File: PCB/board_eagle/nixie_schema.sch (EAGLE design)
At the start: 78 parts, among them IC1 LM2672M, Q1 BC856B, Q2 IRF740S

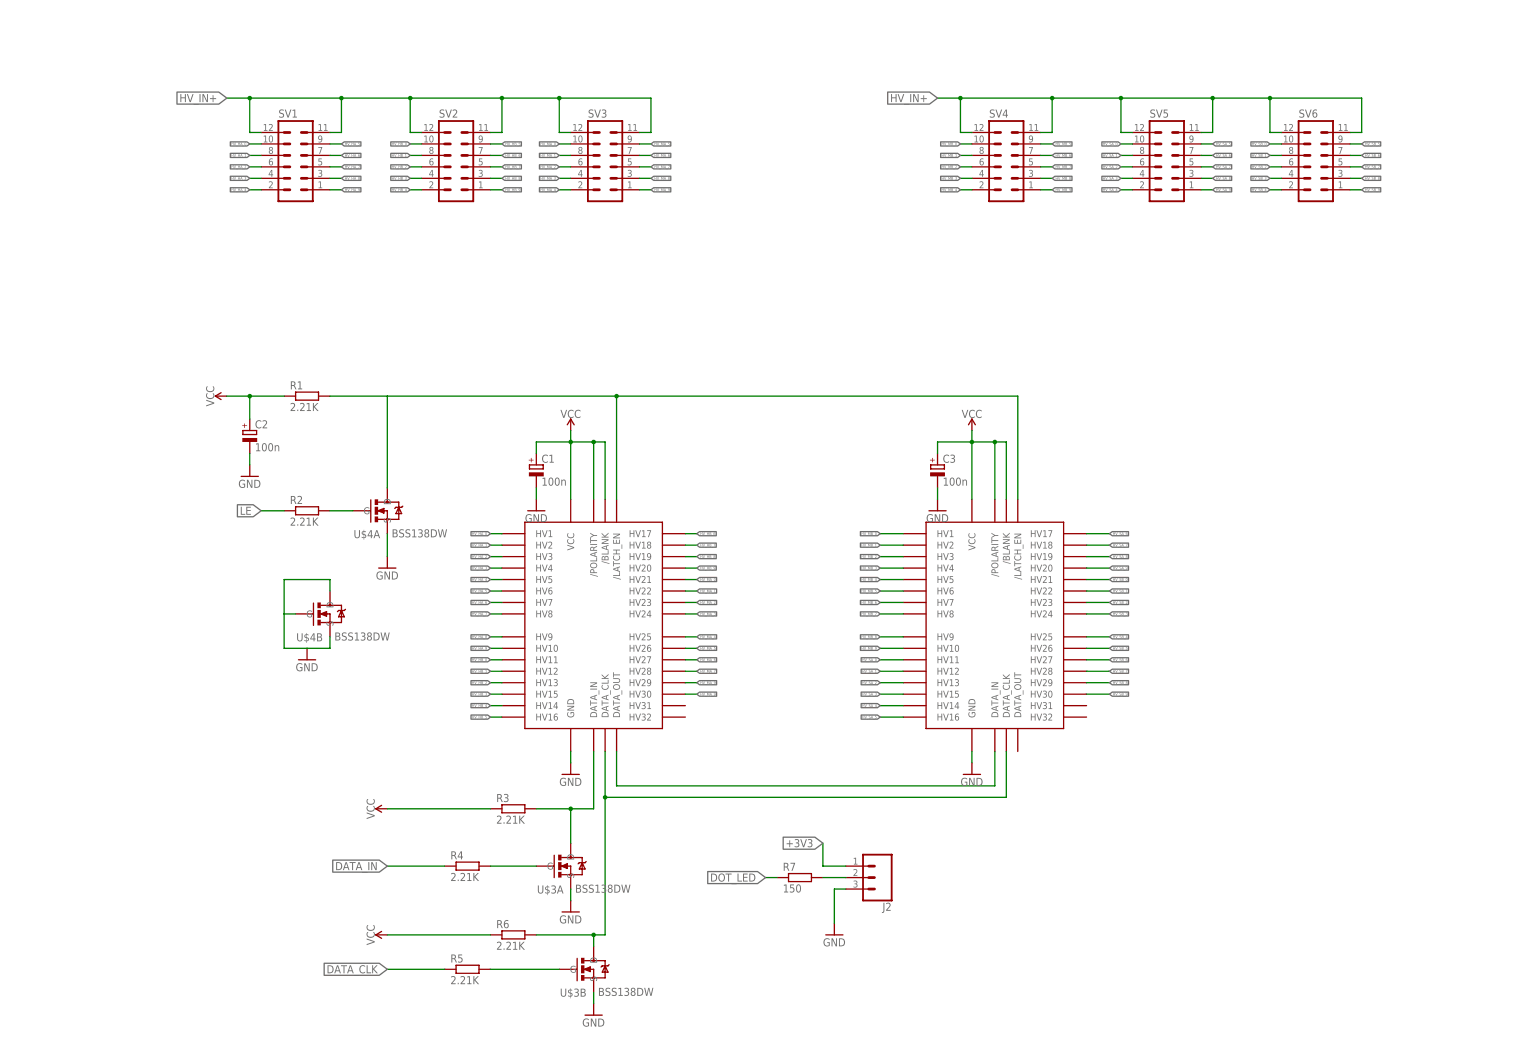
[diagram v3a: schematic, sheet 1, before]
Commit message: Added Buttons
Added 4 buttons and two strip for connectors. buttons are on the last
alb gpios. removed connections for DOT_LED
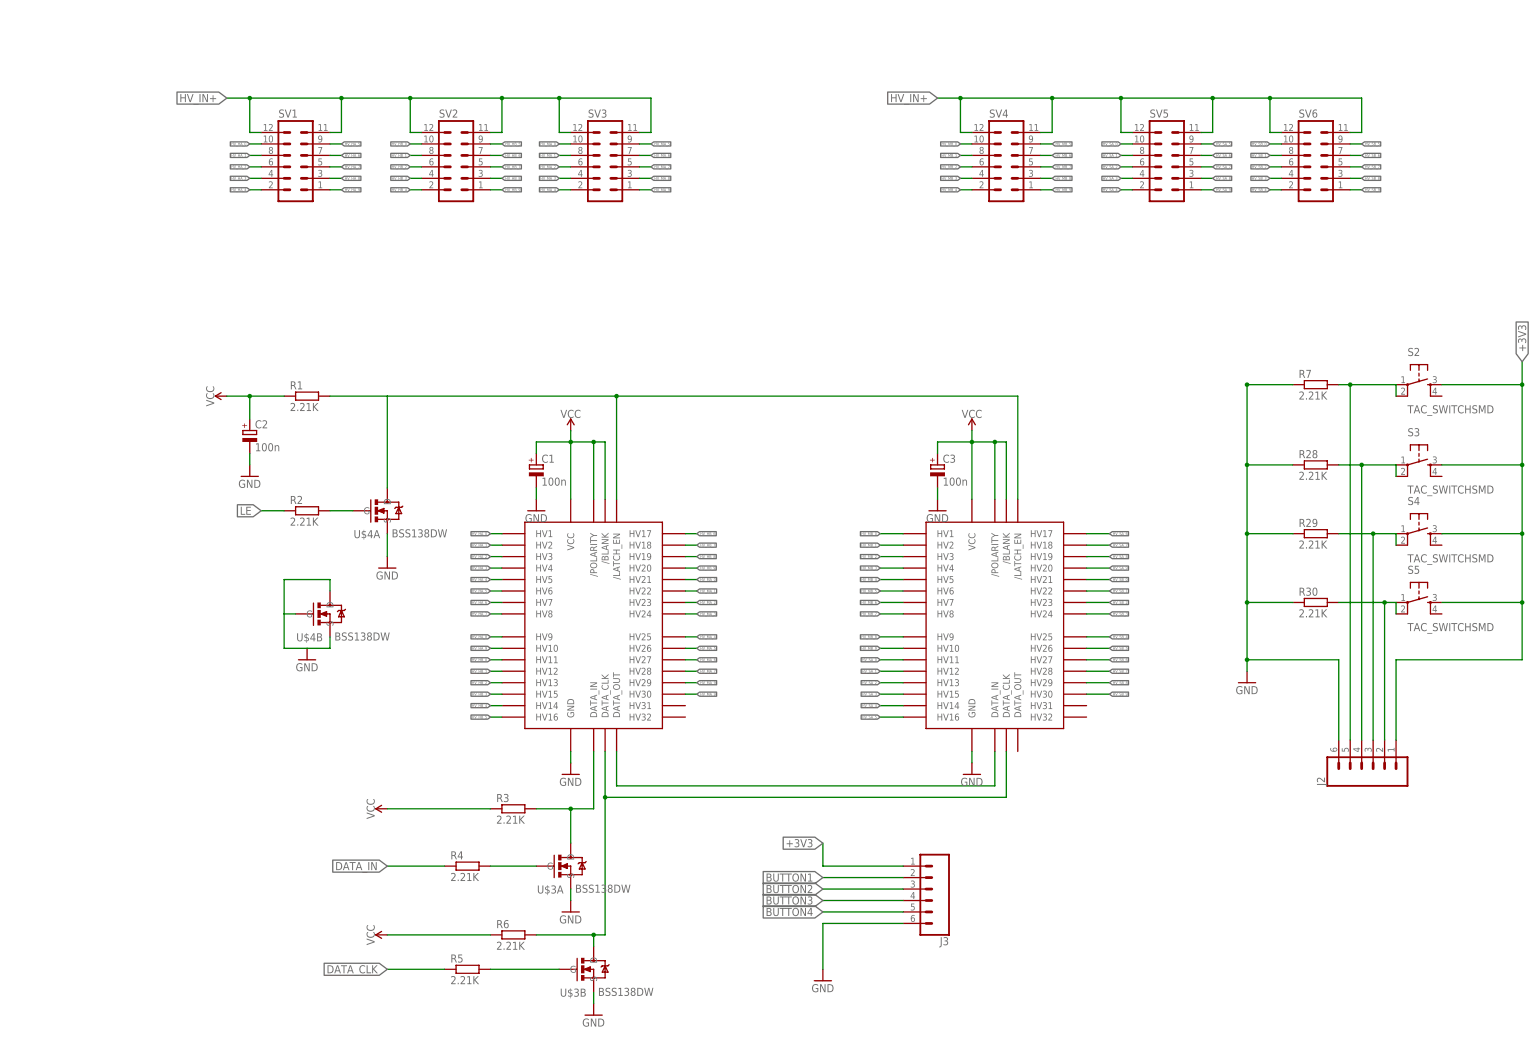
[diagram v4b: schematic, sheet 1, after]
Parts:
- added J3: (no value), SparkFun-Connectors:CONN_06NO_SILK_FEMALE_PTH
- added R28, R29, R30: 2.21K, rcl:R-EU_R0603
- added S2, S3, S4, S5: TAC_SWITCHSMD, SparkFun-Retired:TAC_SWITCHSMD
- J2: device SparkFun-Connectors:CONN_03 -> SparkFun-Connectors:CONN_06NO_SILK_FEMALE_PTH
- R7: value 150 -> 2.21K
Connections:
- removed net DOT_LED: R7.1, U$13.G4
- removed net N$10: J2.2, R7.2
- removed net N$19: U$13.G12
- removed net N$21: U$13.G13
- new net BUTTON1: J2.2, J3.2, R30.2, S5.1, S5.2, U$13.G4
- new net BUTTON2: J2.3, J3.3, R29.2, S4.1, S4.2, U$13.G2
- new net BUTTON3: J2.4, J3.4, R28.2, S3.1, S3.2, U$13.G12
- new net BUTTON4: J2.5, J3.5, R7.2, S2.1, S2.2, U$13.G13
- net +3V3: now also J3.1, S2.3, S3.3, S4.3, S5.3
- net GND: now also J2.6, J3.6, R28.1, R29.1, R30.1, R7.1; no longer J2.3
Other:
- moved on the sheet: R7

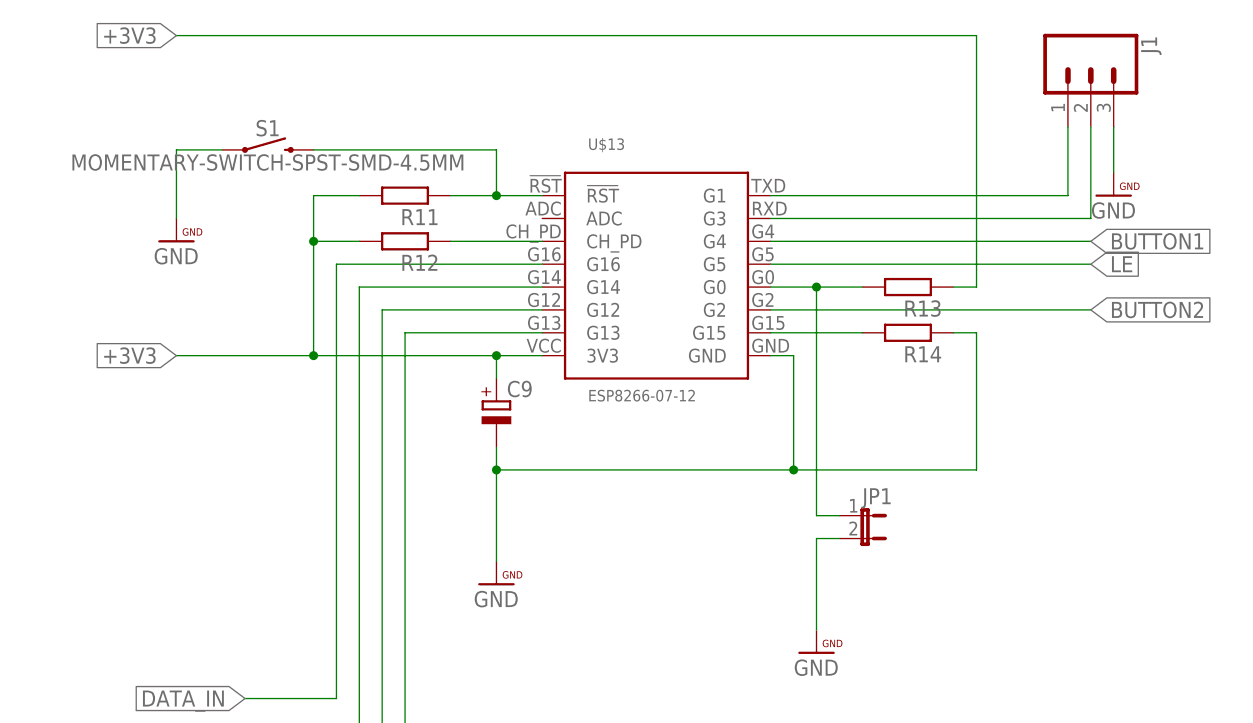
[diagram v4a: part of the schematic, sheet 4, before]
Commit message: Changed ESP8266
changed esp8266 footprint
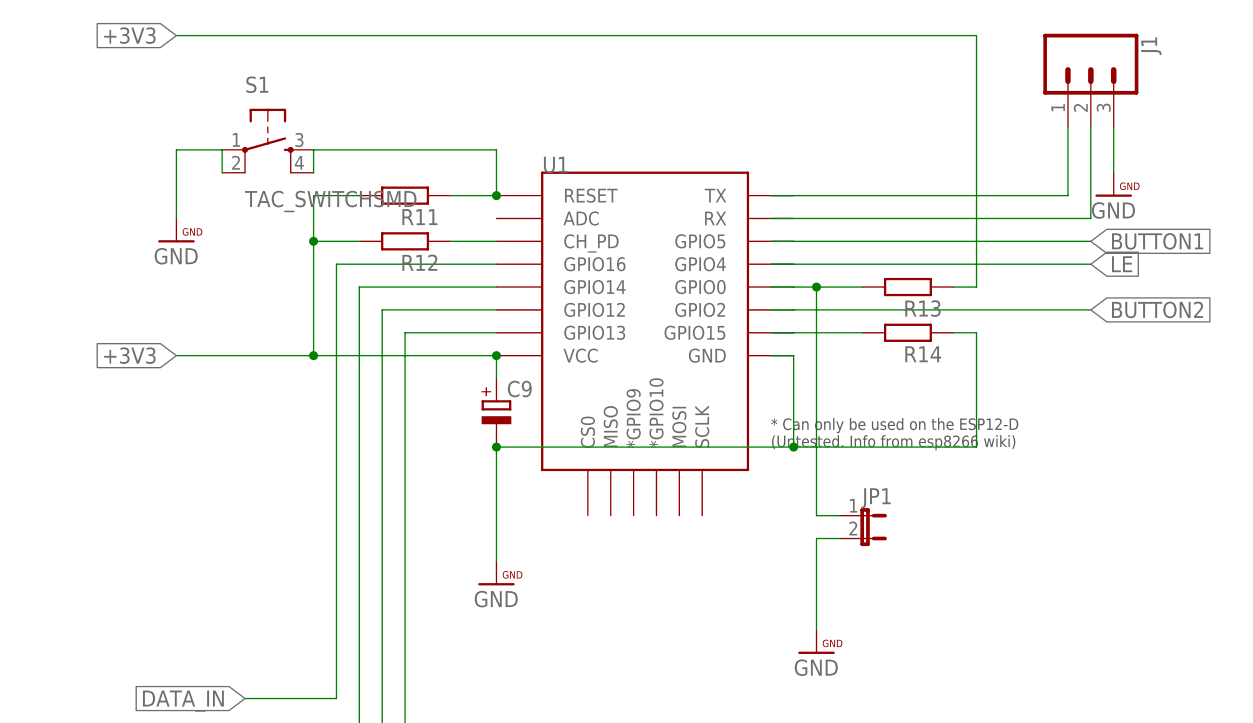
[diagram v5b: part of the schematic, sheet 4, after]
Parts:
- removed U$13: ESP8266-07-12, PatternAgents_RFmodules:ESP8266-07-12
- added U1: (no value), PatternAgents_RFmodules:ESP12ESMD
- S1: value MOMENTARY-SWITCH-SPST-SMD-4.5MM -> TAC_SWITCHSMD; device SparkFun-Switches:MOMENTARY-SWITCH-SPST-SMD-4.5MM -> SparkFun-Retired:TAC_SWITCHSMD
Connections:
- net +3V3: now also U1.VCC; no longer U$13.3V3
- net BUTTON1: now also U1.GPIO5; no longer U$13.G4
- net BUTTON2: now also U1.GPIO2; no longer U$13.G2
- net BUTTON3: now also U1.GPIO12; no longer U$13.G12
- net BUTTON4: now also U1.GPIO13; no longer U$13.G13
- net DATA_CLK: now also U1.GPIO14; no longer U$13.G14
- net DATA_IN: now also U1.GPIO16; no longer U$13.G16
- net GND: now also S1.2, U1.GND; no longer S1.1, U$13.GND
- net LE: now also U1.GPIO4; no longer U$13.G5
- net N$14: now also S1.4, U1.RESET; no longer S1.2, U$13.!RST
- net N$16: now also U1.CH_PD; no longer U$13.CH_PD
- net N$17: now also U1.TX; no longer U$13.G1
- net N$18: now also U1.RX; no longer U$13.G3
- net N$20: now also U1.GPIO15; no longer U$13.G15
- net N$22: now also U1.GPIO0; no longer U$13.G0
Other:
- moved on the sheet: J2

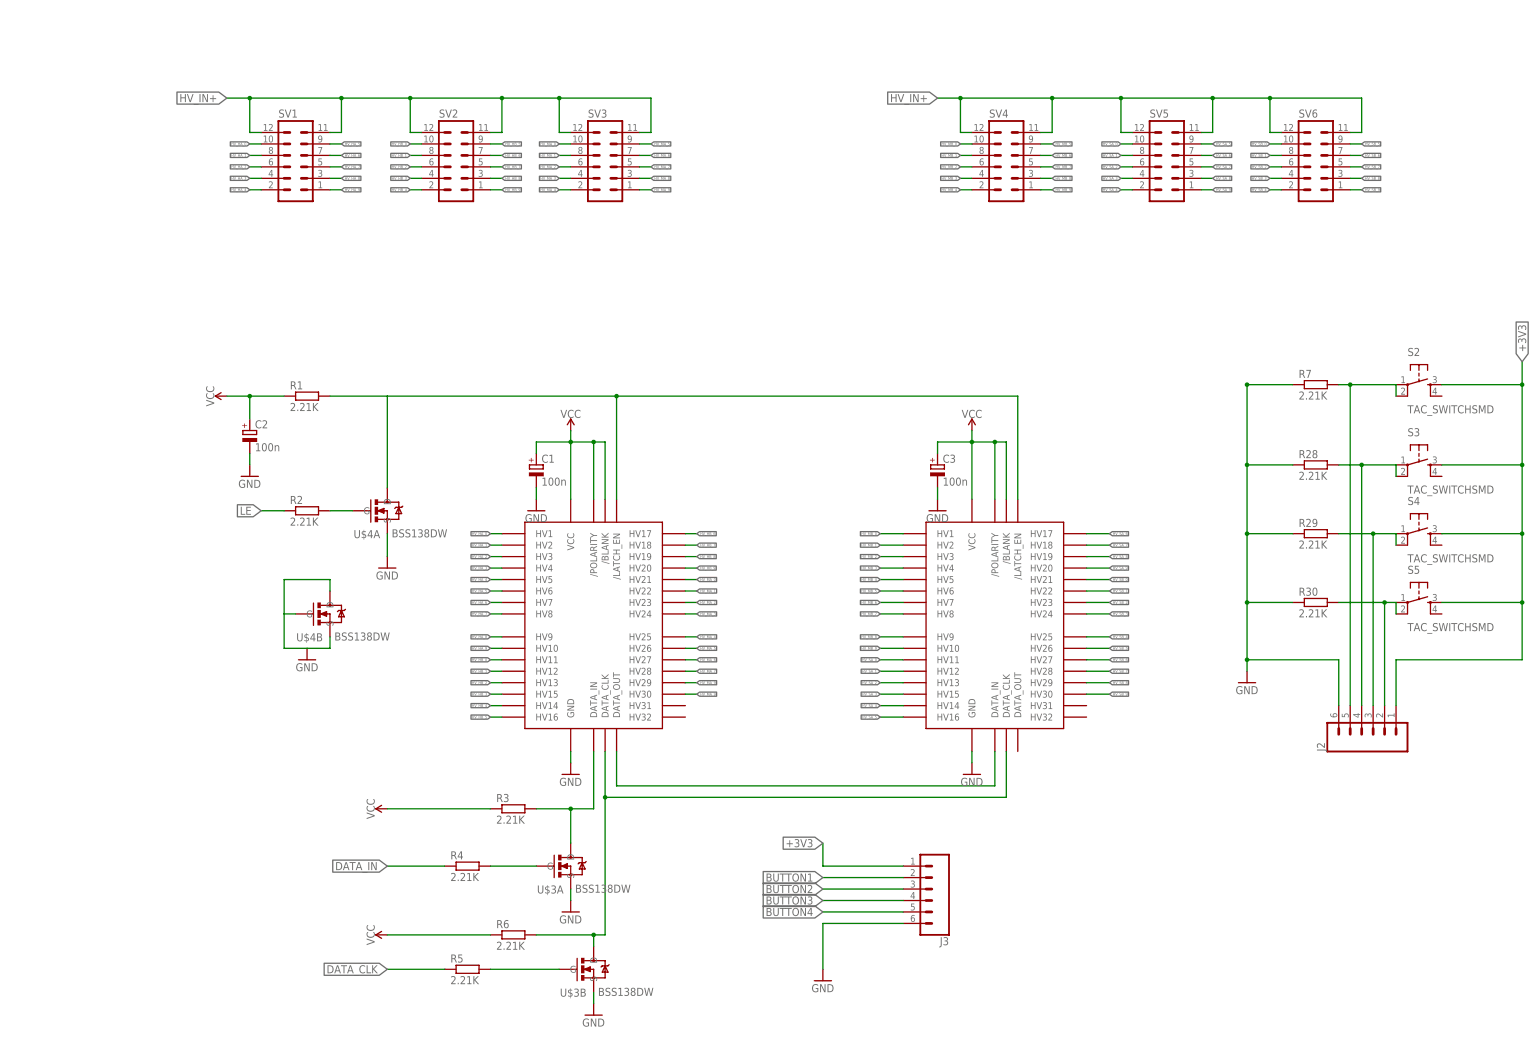
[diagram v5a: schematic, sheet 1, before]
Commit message: Brought Anode resistors to the lower PCB
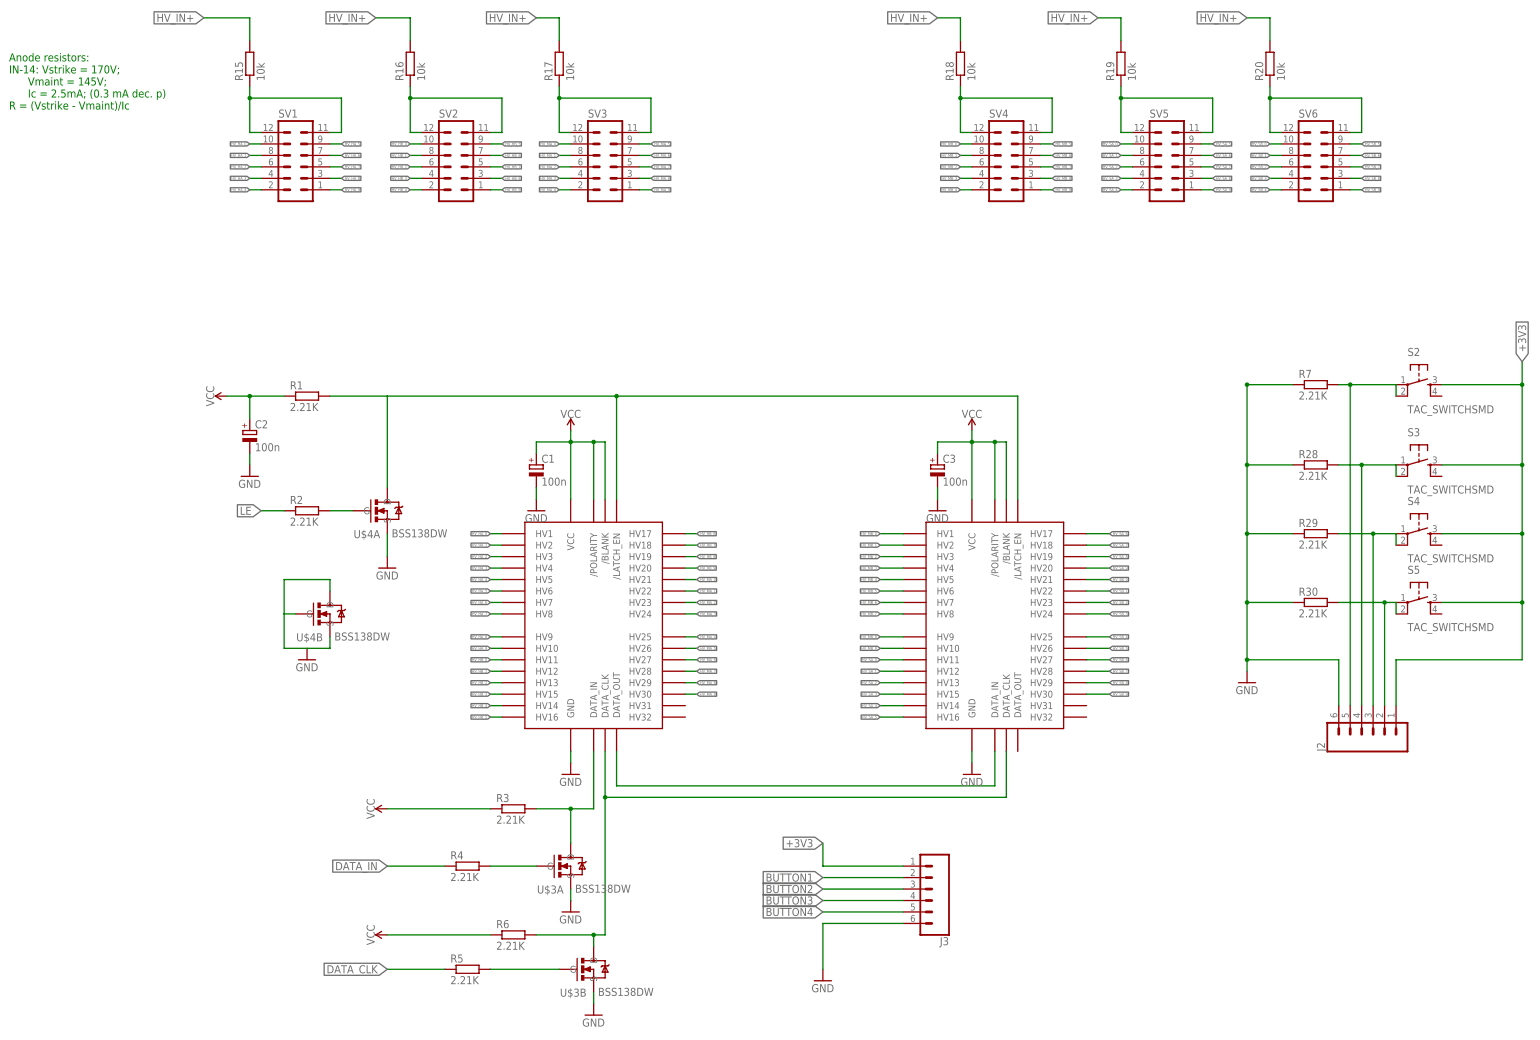
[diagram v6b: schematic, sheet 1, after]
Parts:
- R15, R16, R17, R18, R19, R20: value (none) -> 10k; device resistor:R-EU_R0603 -> rcl:R-EU_R0603
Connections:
- new net N$10: N1.A, SV7.11, SV7.12
- new net N$100: R18.2
- new net N$101: R17.2
- new net N$102: R16.2
- new net N$19: N2.A, SV8.11, SV8.12
- new net N$21: N3.A, SV9.11, SV9.12
- new net N$88: N4.A, SV10.11, SV10.12
- new net N$98: N5.A, SV11.11, SV11.12
- new net N$99: R19.2
- net HV_IN+: now also R17.1, R18.1; no longer SV1.11, SV1.12, SV2.11, SV2.12, SV5.11, SV5.12, SV6.11, SV6.12
- net N$45: now also N6.A; no longer R15.2, R16.2, R17.2, R18.2, R19.2, R20.2, SV10.11, SV10.12, SV11.11, SV11.12, SV7.11, SV7.12, SV8.11, SV8.12, SV9.11, SV9.12
- net N$89: now also R15.1, SV1.11, SV1.12; no longer N6.A, R20.1
- net N$90: now also R16.1, SV2.11, SV2.12; no longer N5.A, R19.1
- net N$91: now also R20.1, SV6.11, SV6.12; no longer N4.A, R18.1
- net N$92: now also R19.1, SV5.11, SV5.12; no longer N3.A, R17.1
- net N$93: now also R15.2; no longer N2.A, R16.1
- net N$94: now also R20.2; no longer N1.A, R15.1
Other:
- note added: "Anode resistors: IN-14: Vstrike = 170V; Vmaint = 145V; Ic = 2.5mA; (0.3 mA dec. p) R = (Vstrike - Vmaint)/Ic"

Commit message: Added cheaper 3V3 PSU
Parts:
- removed C7, C8: 100u, rcl:CPOL-EU140CLH-0810
- removed D5: MBRS130LT3, diode:MBRS130LT3
- removed D6: (no value), SparkFun-LED:LED0603
- removed IC1: LM2672M, v-reg-3:LM2672M
- removed L2: 4.7u, rcl:L-USCEP125
- removed R8: 1.33k, resistor:R-EU_R0603
- added D3: (no value), diode:DIODE-SOD123
- added R32: 5.6k, resistor:R-EU_R0603
- added U$5: MC34063, MC34063:MC34063
- C11: value 680p -> 10n
- C4: value 100u -> 270p; device rcl:CPOL-EU140CLH-0810 -> eagle-ltspice:C
- C5: value 0.01 -> 100u; device Murata_By_element14_Batch_1:GRM31C5C1E104JA01L -> rcl:CPOL-EU153CLV-1014
- C6: value 0.022 -> 100u; device Murata_By_element14_Batch_1:GRM31C5C1E104JA01L -> rcl:CPOL-EU153CLV-1014
- L1: device rcl:L-USCEP125 -> nixe_cmp:HM78D-128151KLFTR
- R10: value (none) -> 3.3k
- R22, R23: value (none) -> 0.5R
- R9: value 2,37K -> 0.5R; device resistor:R-EU_R0603 -> eagle-ltspice:RR1210
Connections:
- removed net N$100: R18.2
- removed net N$101: R17.2
- removed net N$102: R16.2
- removed net N$15: D6.A, R10.2
- removed net N$93: R15.2
- removed net N$94: R20.2
- removed net N$99: R19.2
- new net N$103: R10.1, R32.2, U$5.CMP
- net +3V3: now also C5.+, C6.+, L1.2, R32.1; no longer C8.+, L2.2, R10.1
- net GND: now also C4.2, C5.-, C6.-, D3.A, R10.2, U$5.GND; no longer C4.-, C6.C1, C7.-, C8.-, D5.A, D6.C, IC1.GND, R8.2
- net HV_IN+: now also R15.2, R16.2, R17.2, R18.2, R19.2, R20.2; no longer R17.1, R18.1, SV3.11, SV3.12, SV4.11, SV4.12
- net N$11: now also R17.1, SV3.11, SV3.12; no longer C5.C1, IC1.CB
- net N$12: now also C4.1, U$5.CT; no longer C5.C2, D5.C, IC1.VSW, L1.1, R9.1
- net N$13: now also D3.C, L1.1, U$5.ES; no longer C7.+, L1.2, L2.1
- net N$5: now also R9.2, U$5.CD, U$5.CS, U$5.IS; no longer C6.C2, IC1.SS
- net N$8: now also R18.1, SV4.11, SV4.12; no longer IC1.FB, R8.1, R9.2
- net VCC: now also R9.1, U$5.VCC; no longer C4.+, IC1.VIN
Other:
- note added: "Diode: >1A pk; >0.5A Avg Vr >20 V Preferably Schottly type with as low Vf as possible Second output cap optional Inductor: >0.5A cont, >1A peak >=100 uH"
- note added: "Notes: Q1 generic signal PNP Q2 generic MOSFET >1.5A cont. D1 >300mA cont <4ns recov. D2 >200V brk. 50ns recov.; >300mA cont. C12 <0.3R ESR, 25V C13 >=2.2u; >200V L3 >1.5 A cont"
- note removed: "Notes: Q1 generic signal PNP Q2 generic MOSFET >1.5A cont. D1 >300mA cont <4ns recov. D2 >200V brk. 50ns recov.; >300mA cont. C12 <0.3R ESR, 25V C13 >=2.2u; >200V"
